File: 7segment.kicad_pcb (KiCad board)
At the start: 2 copper layers, 18 x 26 mm, 28 parts, among them J1 Conn_02x05_Counter_Clockwise

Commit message: Maybe fixed?
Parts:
- turned D1 to 0 degrees
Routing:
- net GND: track 52.3 -> 51.0 mm
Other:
- board text added: "revision 2"
- board text removed: "revision 1"

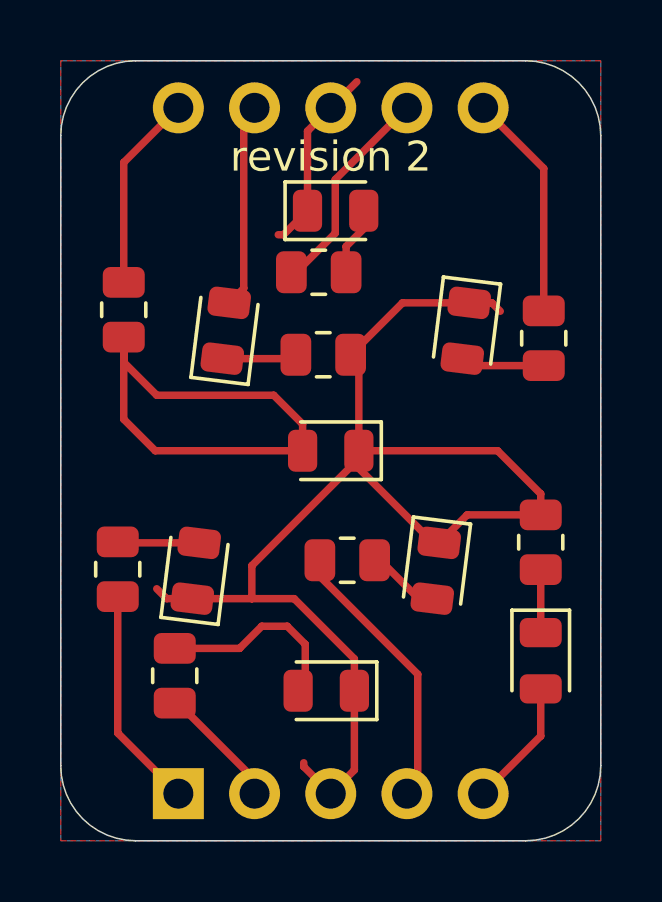
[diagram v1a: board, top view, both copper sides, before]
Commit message: Revision 3, reverse-mount regular 0805 UV LEDs
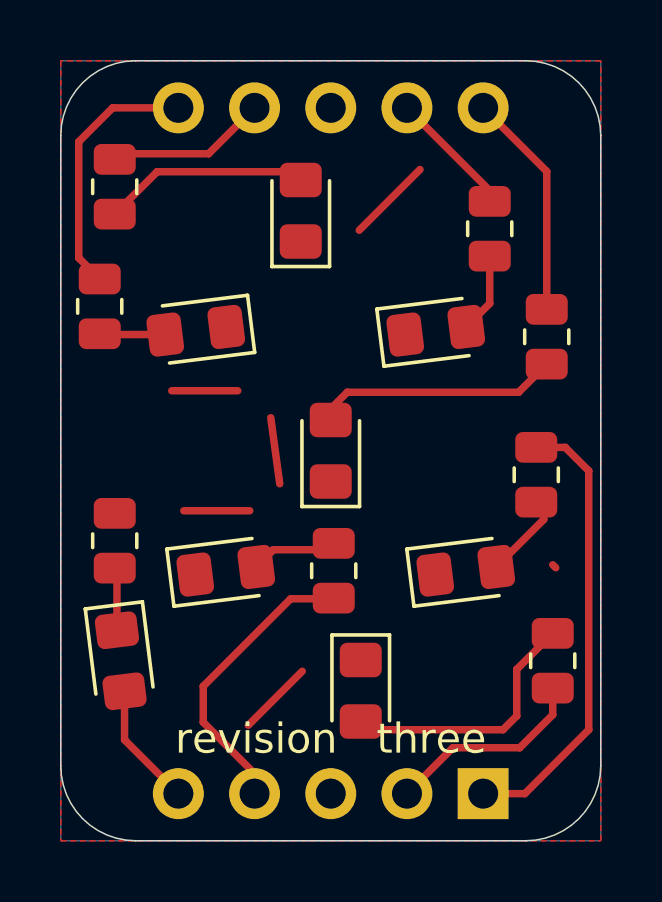
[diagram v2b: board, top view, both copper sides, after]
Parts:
- D1, D2, D3, D4, D5, D6, D7, D8: footprint LED_SMD:LED_0805_2012Metric -> LED_SMD:LED_0805_2012Metric_Pad1.15x1.40mm_HandSolder
- J1: moved to B.Cu
- moved REF** 19.8 mm to (102.0, 94.0), turned to 0 degrees (x2)
- moved REF** 17.7 mm to (103.7, 94.1), turned to 0 degrees
- moved R2 14.8 mm to (101.3, 82.2)
- moved R5 14.3 mm to (115.8, 87.8), turned to 90 degrees
- moved R8 14.2 mm to (101.8, 90.0)
- moved R7 14.1 mm to (116.2, 83.2)
- moved D7 14.0 mm to (102.0, 94.0), turned to 277.1 degrees
- moved R4 12.6 mm to (116.4, 94.0)
- moved J1 10.2 mm to (114.1, 98.4)
- moved D2 9.00 mm to (104.5, 83.0), turned to 187.1 degrees
- moved D5 9.00 mm to (113.5, 91.0), turned to 7.1 degrees
- moved R1 7.37 mm to (101.8, 78.2), turned to 90 degrees
- moved D3 7.00 mm to (112.5, 83.0), turned to 7.1 degrees
- moved D6 7.00 mm to (105.5, 91.0), turned to 7.1 degrees
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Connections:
- D3 pad 1: F -> GND
- D3 pad 2: 9 -> F
- R6 pad 1: GND -> F
- R6 pad 2: F -> 9
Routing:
- net GND: track 51.0 -> 12.7 mm
- net G: track 17.7 -> 8.25 mm
- net 1: track 7.40 -> 14.9 mm
- net A: track 2.29 -> 6.78 mm
- net 2: track 4.19 -> 6.84 mm
- net 9: track 6.85 -> 4.26 mm
- net D: track 6.55 -> 8.63 mm
- net 7: track 7.17 -> 5.37 mm
- net 6: track 7.60 -> 8.65 mm
- net 10: track 6.57 -> 7.60 mm
- net E: track 2.73 -> 3.43 mm
- net B: track 2.81 -> 2.19 mm
- net 4: track 9.28 -> 9.86 mm
- added copper zone on F.Cu, net (none)
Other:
- board text added: "revision three"
- board text removed: "revision 2"

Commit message: Ready to publish?
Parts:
- moved REF** 0.15 mm to (105.1, 86.0)
- moved REF** 0.15 mm to (112.9, 88.0)
- moved REF** 0.15 mm to (112.7, 86.0)
- moved REF** 0.15 mm to (105.3, 88.0)
- turned REF** to 45 degrees (x2)
- turned REF** to 97.1 degrees
- turned REF** to 135 degrees (x2)
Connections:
- REF** pad : (no net) -> GND (x9)
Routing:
- net GND: track 12.7 -> 36.9 mm
- net 4: track 9.86 -> 7.61 mm
- added copper zone on B.Cu, net GND
- removed copper zone on B.Cu, net (none)
- removed copper zone on F.Cu, net (none)
